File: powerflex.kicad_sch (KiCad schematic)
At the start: 2 parts, among them CN18 DF40C-20DS-0.4V, CN19 DF40C-20DS-0.4V

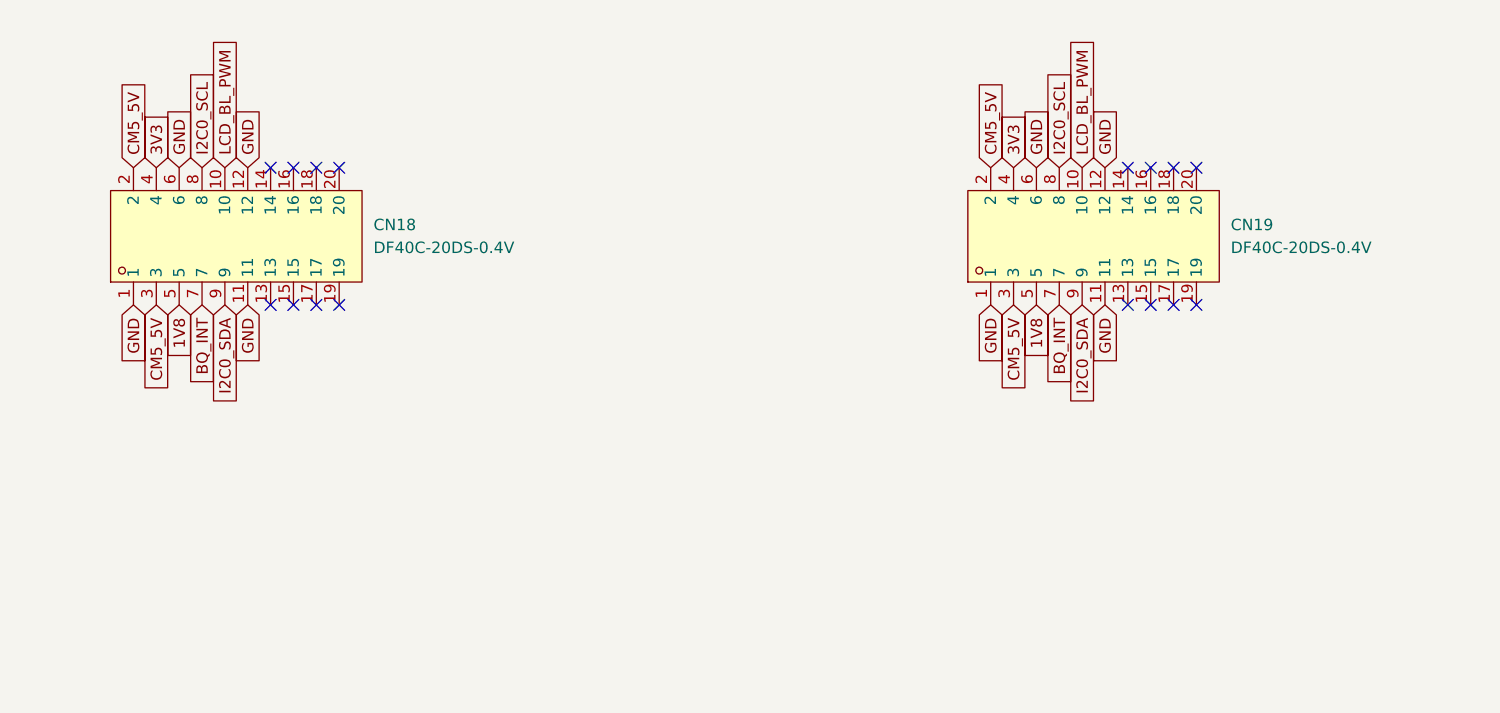
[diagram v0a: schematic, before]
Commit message: finished slateconnect i2c gpio expander, completed led status bar schematic, fixed all drc errors, started assigning footprints and started bom
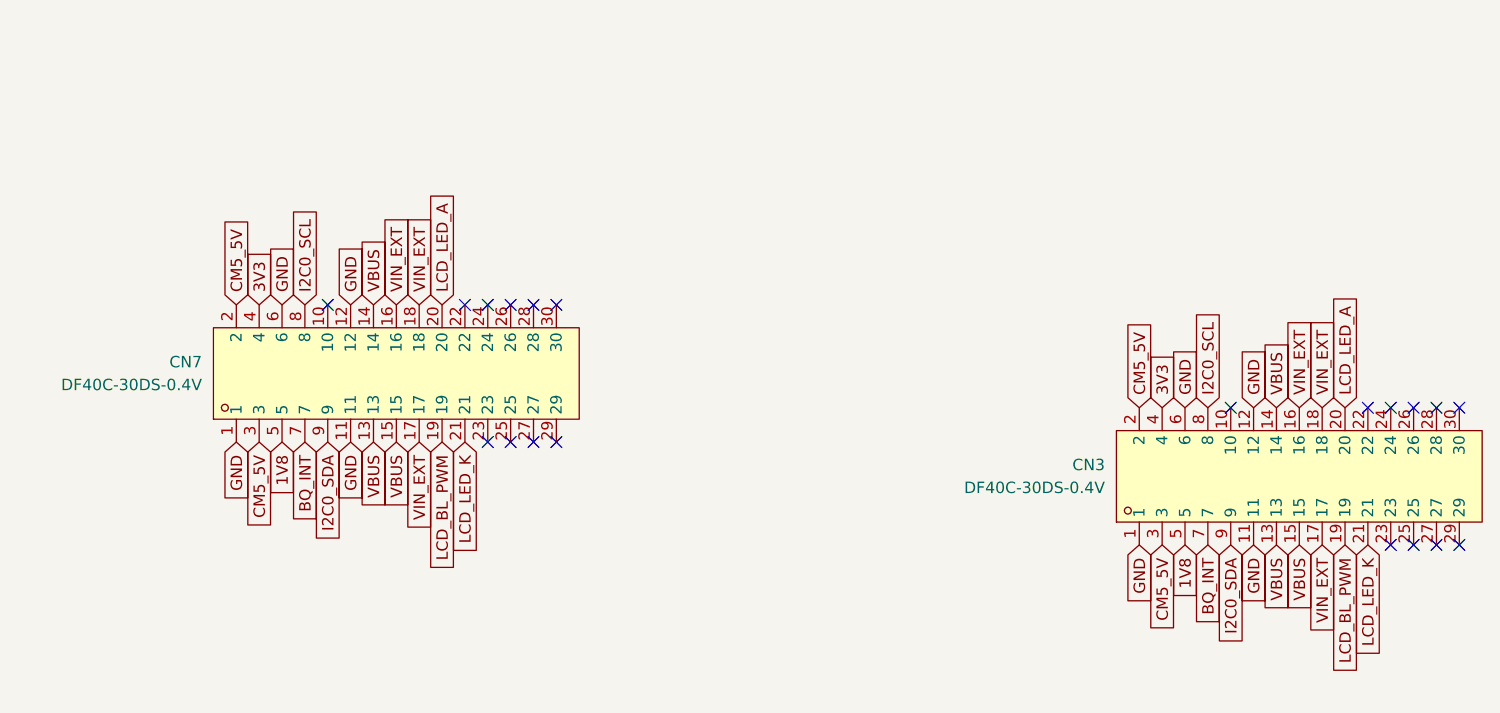
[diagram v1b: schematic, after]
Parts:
- removed CN18, CN19: DF40C-20DS-0.4V, slate113:CONN-SMD_20P-P0.40_DF40C-20DS-0.4V, symbol slate113:DF40C-20DS-0.4V
- added CN3, CN7: DF40C-30DS-0.4V, slate113:CONN-SMD_DF40C-30DS-0.4V51, symbol slate113:DF40C-30DS-0.4V
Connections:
- net 1V8: now also CN3.5, CN7.5
- net 3V3: now also CN3.4, CN7.4
- net BQ_INT: now also CN3.7, CN7.7
- net CM5_5V: now also CN3.2, CN3.3, CN7.2, CN7.3
- net GND: now also CN3.1, CN3.11, CN3.12, CN3.6, CN7.1, CN7.11, CN7.12, CN7.6
- net I2C0_SCL: now also CN3.8, CN7.8
- net I2C0_SDA: now also CN3.9, CN7.9
- net LCD_BL_PWM: now also CN3.19, CN7.19
- new net LCD_LED_A: CN3.20, CN7.20
- new net LCD_LED_K: CN3.21, CN7.21
- new net VBUS: CN3.13, CN3.14, CN3.15, CN7.13, CN7.14, CN7.15
- new net VIN_EXT: CN3.16, CN3.17, CN3.18, CN7.16, CN7.17, CN7.18
- no-connect marks 16 -> 20

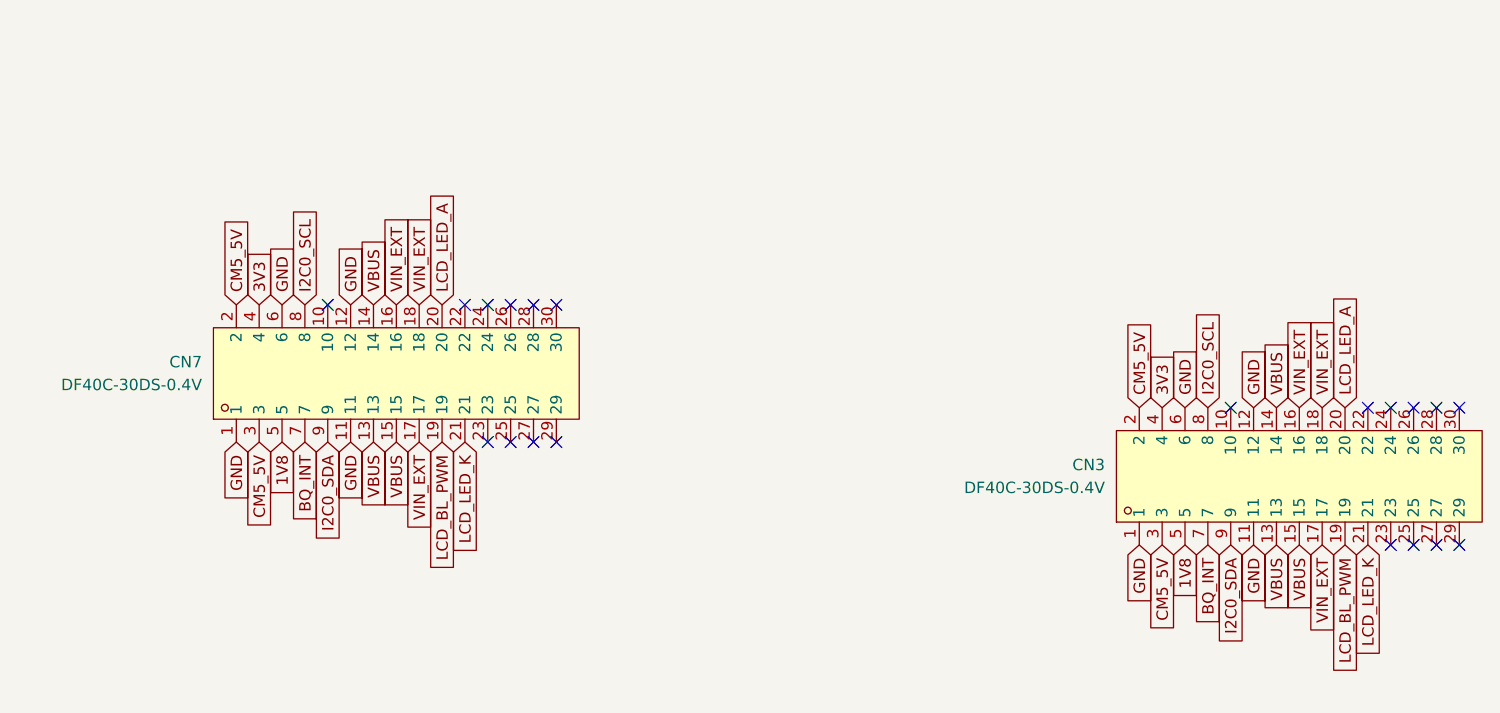
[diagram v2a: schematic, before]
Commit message: imported footprints and 3d models, replaced obsolete components, finished schematic audit, wired new usb hub and flash chip + more, removed stale nets
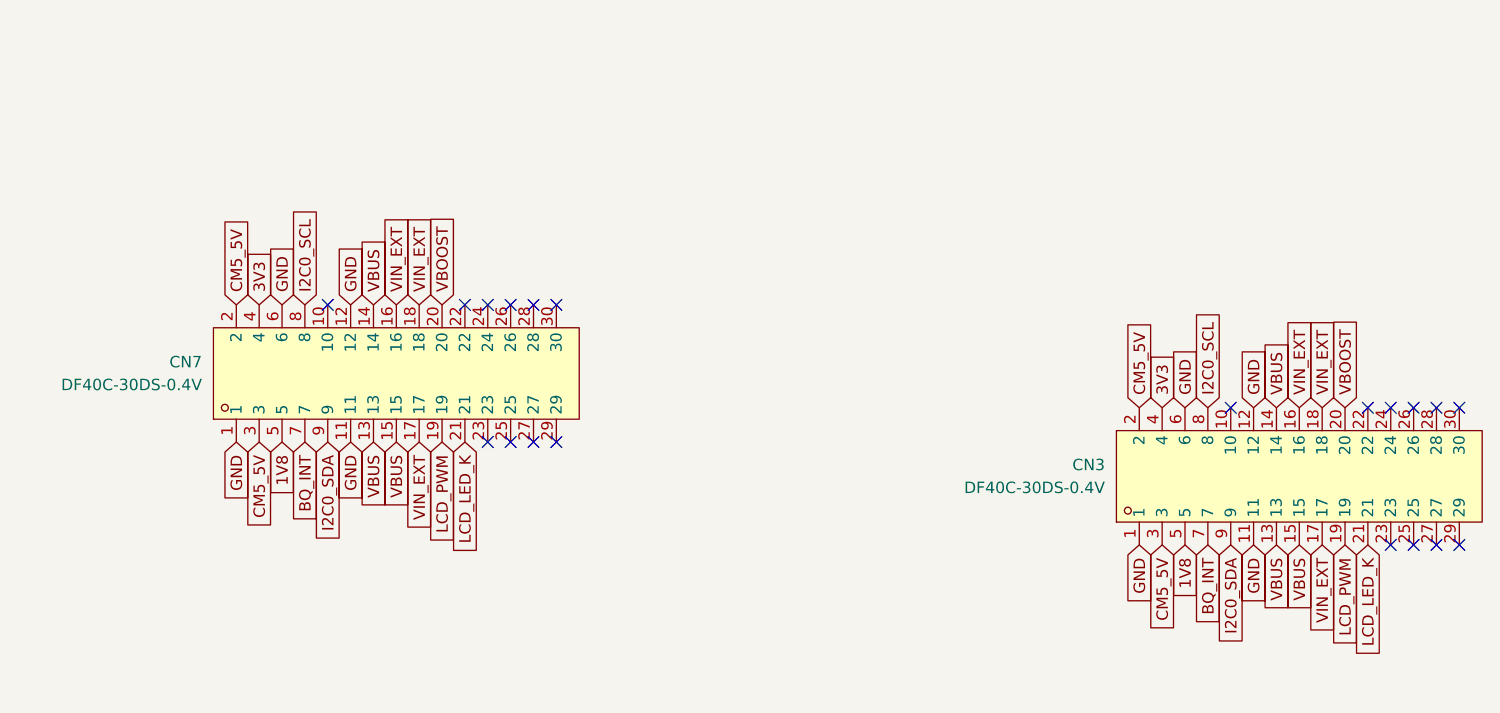
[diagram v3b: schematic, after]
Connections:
- net LCD_BL_PWM renamed LCD_PWM
- net LCD_LED_A renamed VBOOST
